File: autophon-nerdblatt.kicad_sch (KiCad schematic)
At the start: 21 parts, among them J101 board-edge-connector, U101 LM1117-3.3, U102 LM2594M-5.0

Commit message: New Footprint for L
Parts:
- L101: footprint Inductor_SMD:L_1210_3225Metric -> Inductor_SMD:L_Bourns-SRN8040_8x8.15mm; Link https://www.reichelt.de/smd-induktivitaet-1210-murata-chip-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 -> https://www.reichelt.de/smd-power-induktivitaet-100-h-eaton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
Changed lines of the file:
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@@
   (junction (at 248.92 38.1) (diameter 1.016) (color 0 0 0 0))
   (junction (at 257.81 38.1) (diameter 1.016) (color 0 0 0 0))
+  (no_connect (at 87.63 147.32))
+  (no_connect (at 111.76 124.46))
+  (no_connect (at 87.63 50.8))
+  (no_connect (at 111.76 50.8))
+  (no_connect (at 111.76 152.4))
+  (no_connect (at 111.76 81.28))
+  (no_connect (at 87.63 160.02))
+  (no_connect (at 111.76 99.06))
+  (no_connect (at 111.76 48.26))
+  (no_connect (at 87.63 101.6))
   (no_connect (at 111.76 58.42))
+  (no_connect (at 111.76 76.2))
+  (no_connect (at 87.63 48.26))
+  (no_connect (at 87.63 83.82))
+  (no_connect (at 111.76 91.44))
+  (no_connect (at 111.76 157.48))
+  (no_connect (at 87.63 81.28))
+  (no_connect (at 111.76 109.22))
+  (no_connect (at 87.63 68.58))
+  (no_connect (at 87.63 114.3))
+  (no_connect (at 87.63 144.78))
+  (no_connect (at 87.63 55.88))
+  (no_connect (at 87.63 76.2))
+  (no_connect (at 87.63 63.5))
+  (no_connect (at 111.76 55.88))
+  (no_connect (at 87.63 58.42))
+  (no_connect (at 87.63 134.62))
+  (no_connect (at 87.63 157.48))
+  (no_connect (at 87.63 154.94))
+  (no_connect (at 87.63 99.06))
+  (no_connect (at 111.76 86.36))
+  (no_connect (at 87.63 78.74))
+  (no_connect (at 87.63 53.34))
+  (no_connect (at 87.63 149.86))
+  (no_connect (at 87.63 91.44))
+  (no_connect (at 111.76 154.94))
+  (no_connect (at 111.76 88.9))
+  (no_connect (at 111.76 93.98))
+  (no_connect (at 111.76 53.34))
+  (no_connect (at 87.63 88.9))
+  (no_connect (at 111.76 96.52))
+  (no_connect (at 87.63 152.4))
+  (no_connect (at 111.76 144.78))
+  (no_connect (at 111.76 101.6))
+  (no_connect (at 111.76 83.82))
+  (no_connect (at 87.63 96.52))
+  (no_connect (at 111.76 106.68))
+  (no_connect (at 87.63 124.46))
+  (no_connect (at 111.76 149.86))
+  (no_connect (at 111.76 63.5))
+  (no_connect (at 111.76 142.24))
+  (no_connect (at 111.76 147.32))
+  (no_connect (at 111.76 68.58))
+  (no_connect (at 111.76 78.74))
+  (no_connect (at 111.76 121.92))
+  (no_connect (at 87.63 93.98))
+  (no_connect (at 87.63 86.36))
   (no_connect (at 111.76 160.02))
-  (no_connect (at 87.63 55.88))
-  (no_connect (at 111.76 157.48))
-  (no_connect (at 111.76 91.44))
-  (no_connect (at 87.63 58.42))
-  (no_connect (at 111.76 68.58))
-  (no_connect (at 87.63 99.06))
-  (no_connect (at 87.63 144.78))
-  (no_connect (at 111.76 48.26))
-  (no_connect (at 111.76 101.6))
-  (no_connect (at 87.63 86.36))
-  (no_connect (at 87.63 154.94))
-  (no_connect (at 111.76 78.74))
-  (no_connect (at 87.63 83.82))
-  (no_connect (at 111.76 83.82))
-  (no_connect (at 111.76 96.52))
-  (no_connect (at 87.63 160.02))
-  (no_connect (at 111.76 93.98))
-  (no_connect (at 111.76 106.68))
-  (no_connect (at 111.76 76.2))
-  (no_connect (at 111.76 99.06))
-  (no_connect (at 87.63 53.34))
-  (no_connect (at 87.63 114.3))
-  (no_connect (at 87.63 157.48))
-  (no_connect (at 87.63 96.52))
-  (no_connect (at 111.76 81.28))
-  (no_connect (at 87.63 68.58))
-  (no_connect (at 111.76 124.46))
-  (no_connect (at 87.63 76.2))
-  (no_connect (at 87.63 78.74))
-  (no_connect (at 87.63 81.28))
-  (no_connect (at 87.63 134.62))
-  (no_connect (at 111.76 88.9))
-  (no_connect (at 111.76 86.36))
-  (no_connect (at 111.76 154.94))
-  (no_connect (at 111.76 55.88))
-  (no_connect (at 111.76 109.22))
-  (no_connect (at 111.76 149.86))
-  (no_connect (at 87.63 50.8))
-  (no_connect (at 111.76 147.32))
-  (no_connect (at 111.76 152.4))
-  (no_connect (at 111.76 121.92))
-  (no_connect (at 87.63 101.6))
-  (no_connect (at 111.76 53.34))
-  (no_connect (at 111.76 63.5))
-  (no_connect (at 111.76 144.78))
-  (no_connect (at 87.63 147.32))
-  (no_connect (at 87.63 91.44))
-  (no_connect (at 87.63 48.26))
-  (no_connect (at 87.63 63.5))
-  (no_connect (at 87.63 149.86))
-  (no_connect (at 87.63 124.46))
-  (no_connect (at 87.63 93.98))
-  (no_connect (at 111.76 50.8))
-  (no_connect (at 87.63 152.4))
-  (no_connect (at 87.63 88.9))
-  (no_connect (at 111.76 142.24))
   (wire (pts (xy 77.47 57.15) (xy 77.47 59.69))
     (stroke (width 0) (type solid) (color 0 0 0 0))
@@
     )
   )
-  (symbol (lib_id "power:+24V") (at 77.47 57.15 0)
+  (symbol (lib_id "power:+24V") (at 77.47 57.15 0) (unit 1)
     (in_bom yes) (on_board yes)
     (property "Reference" "#PWR0109" (id 0) (at 77.47 60.96 0)
@@
     )
   )
-  (symbol (lib_id "power:+24V") (at 152.4 24.13 0)
+  (symbol (lib_id "power:+24V") (at 152.4 24.13 0) (unit 1)
     (in_bom yes) (on_board yes)
     (property "Reference" "#PWR0104" (id 0) (at 152.4 27.94 0)
@@
     )
   )
-  (symbol (lib_id "power:+5V") (at 209.55 24.13 0)
+  (symbol (lib_id "power:+5V") (at 209.55 24.13 0) (unit 1)
     (in_bom yes) (on_board yes)
     (property "Reference" "#PWR0105" (id 0) (at 209.55 27.94 0)
@@
     )
   )
-  (symbol (lib_id "power:VCC") (at 233.68 24.13 0)
+  (symbol (lib_id "power:VCC") (at 233.68 24.13 0) (unit 1)
     (in_bom yes) (on_board yes)
     (property "Reference" "#PWR0106" (id 0) (at 233.68 27.94 0)
@@
     )
   )
-  (symbol (lib_id "power:+24V") (at 248.92 17.78 0)
+  (symbol (lib_id "power:+24V") (at 248.92 17.78 0) (unit 1)
     (in_bom yes) (on_board yes)
     (property "Reference" "#PWR0101" (id 0) (at 248.92 21.59 0)
@@
     )
   )
-  (symbol (lib_id "power:+5V") (at 257.81 17.78 0)
+  (symbol (lib_id "power:+5V") (at 257.81 17.78 0) (unit 1)
     (in_bom yes) (on_board yes)
     (property "Reference" "#PWR0102" (id 0) (at 257.81 21.59 0)
@@
     )
   )
-  (symbol (lib_id "power:VCC") (at 266.7 17.78 0)
+  (symbol (lib_id "power:VCC") (at 266.7 17.78 0) (unit 1)
     (in_bom yes) (on_board yes)
     (property "Reference" "#PWR0103" (id 0) (at 266.7 21.59 0)
@@
     )
   )
-  (symbol (lib_id "Device:L") (at 195.58 27.94 90)
+  (symbol (lib_id "Device:L") (at 195.58 27.94 90) (unit 1)
     (in_bom yes) (on_board yes)
     (property "Reference" "L101" (id 0) (at 195.58 41.91 90))
     (property "Value" "100uH" (id 1) (at 195.58 44.45 90))
-    (property "Footprint" "Inductor_SMD:L_1210_3225Metric" (id 2) (at 195.58 27.94 0)
+    (property "Footprint" "Inductor_SMD:L_Bourns-SRN8040_8x8.15mm" (id 2) (at 195.58 27.94 0)
       (effects (font (size 1.27 1.27)) hide)
     )
@@
       (effects (font (size 1.27 1.27)) hide)
     )
-    (property "Link" "https://www.reichelt.de/smd-induktivitaet-1210-murata-chip-coil-100--lqh3c-100--p10555.html?&trstct=pos_0&nbc=1" (id 5) (at 195.58 27.94 0)
+    (property "Link" "https://www.reichelt.de/smd-power-induktivitaet-100-h-eaton-dr74-101-r-p245727.html?&trstct=pos_10&nbc=1" (id 5) (at 195.58 27.94 0)
       (effects (font (size 1.27 1.27)) hide)
     )
@@
     )
   )
-  (symbol (lib_id "Device:CP") (at 153.67 33.02 0)
+  (symbol (lib_id "Device:CP") (at 153.67 33.02 0) (unit 1)
     (in_bom yes) (on_board yes)
     (property "Reference" "C101" (id 0) (at 152.4 41.91 0)
@@
     )
   )
-  (symbol (lib_id "Device:C") (at 161.29 33.02 0)
+  (symbol (lib_id "Device:C") (at 161.29 33.02 0) (unit 1)
     (in_bom yes) (on_board yes)
     (property "Reference" "C102" (id 0) (at 160.02 41.91 0)
@@
     )
   )
-  (symbol (lib_id "Device:CP") (at 201.93 33.02 0)
+  (symbol (lib_id "Device:CP") (at 201.93 33.02 0) (unit 1)
     (in_bom yes) (on_board yes)
     (property "Reference" "C103" (id 0) (at 200.66 41.91 0)
@@
     )
   )
-  (symbol (lib_id "Device:C") (at 208.28 33.02 0)
+  (symbol (lib_id "Device:C") (at 208.28 33.02 0) (unit 1)
     (in_bom yes) (on_board yes)
     (property "Reference" "C104" (id 0) (at 207.01 41.91 0)
@@
     )
   )
-  (symbol (lib_id "Device:CP") (at 214.63 33.02 0)
+  (symbol (lib_id "Device:CP") (at 214.63 33.02 0) (unit 1)
     (in_bom yes) (on_board yes)
     (property "Reference" "C105" (id 0) (at 213.36 41.91 0)
@@
     )
   )
-  (symbol (lib_id "Device:CP") (at 232.41 33.02 0)
+  (symbol (lib_id "Device:CP") (at 232.41 33.02 0) (unit 1)
     (in_bom yes) (on_board yes)
     (property "Reference" "C106" (id 0) (at 231.14 41.91 0)
@@
     )
   )
-  (symbol (lib_id "Device:CP") (at 238.76 33.02 0)
+  (symbol (lib_id "Device:CP") (at 238.76 33.02 0) (unit 1)
     (in_bom yes) (on_board yes)
     (property "Reference" "C107" (id 0) (at 237.49 41.91 0)
@@
     )
   )
-  (symbol (lib_id "Regulator_Switching:LM2594M-5.0") (at 179.07 27.94 0)
+  (symbol (lib_id "Regulator_Switching:LM2594M-5.0") (at 179.07 27.94 0) (unit 1)
     (in_bom yes) (on_board yes)
     (property "Reference" "U102" (id 0) (at 179.07 18.6182 0))
@@
     )
     (path "/00000000-0000-0000-0000-00006024446a"
-      (reference "L101") (unit 1) (value "100uH") (footprint "Inductor_SMD:L_1210_3225Metric")
+      (reference "L101") (unit 1) (value "100uH") (footprint "Inductor_SMD:L_Bourns-SRN8040_8x8.15mm")
     )
     (path "/00000000-0000-0000-0000-00006025e2b0"

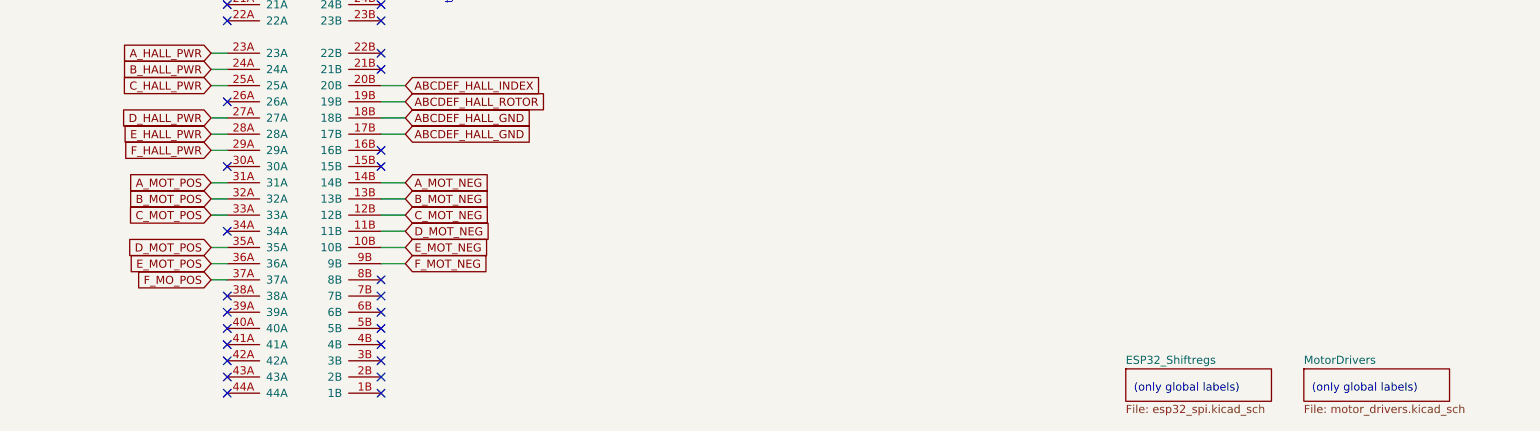
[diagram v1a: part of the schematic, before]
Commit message: more C vor Logic and placing first groups of parts
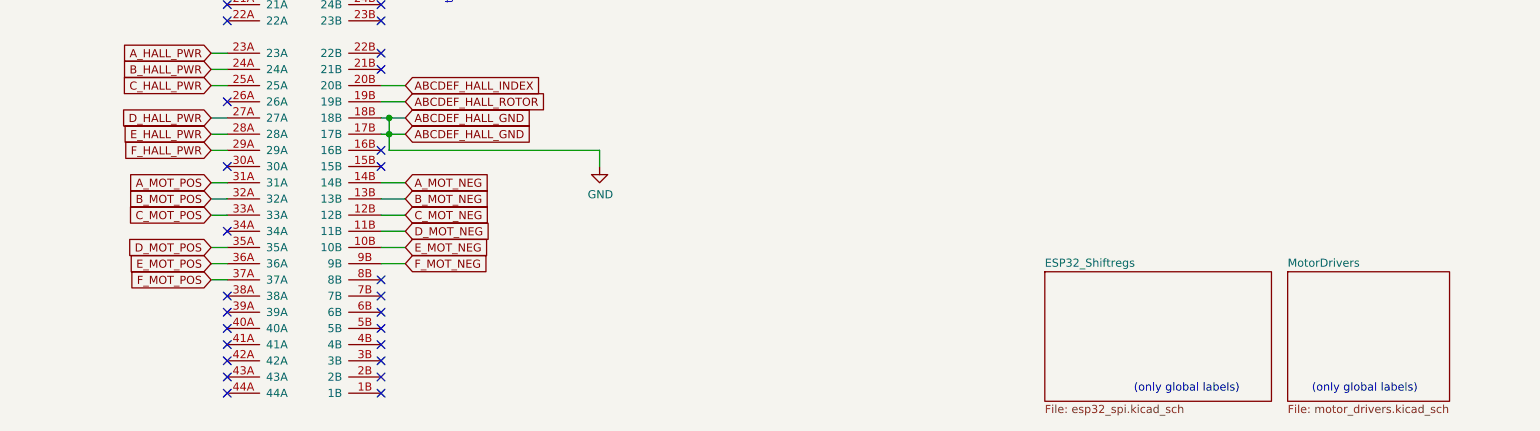
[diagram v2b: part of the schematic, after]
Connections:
- net ABCDEF_HALL_GND is gone; now on net GND: J101.17B, J101.18B
- net F_MO_POS renamed F_MOT_POS

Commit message: all traces routed. ready for cleanup
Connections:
- net GND: now also C105.2, C106.2, C107.2, D101.1 (K), D102.1 (K), D103.1 (K), U101.1 (GND)
